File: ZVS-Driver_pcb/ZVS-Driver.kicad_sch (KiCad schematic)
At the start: 25 parts, among them J1 Screw_Terminal_01x02, J3 Screw_Terminal_01x04, Q1 IRF540N, Q2 IRF540N, Q3 IRF540N, Q4 IRF540N, Q5 IRF540N

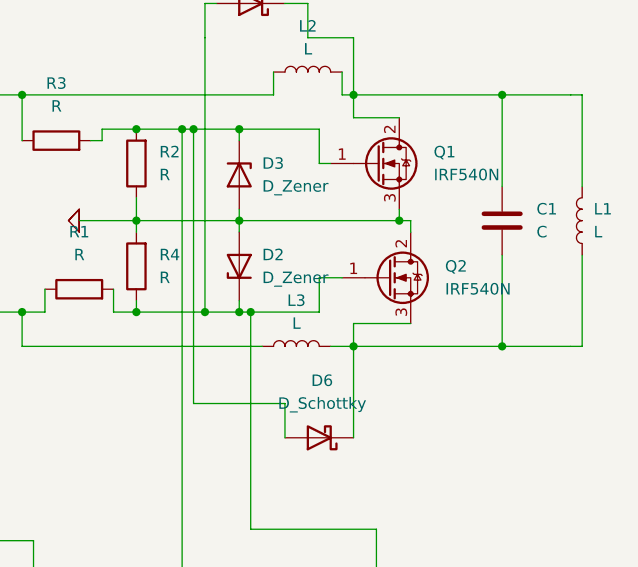
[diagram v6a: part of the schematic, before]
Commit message: Mosfet fix
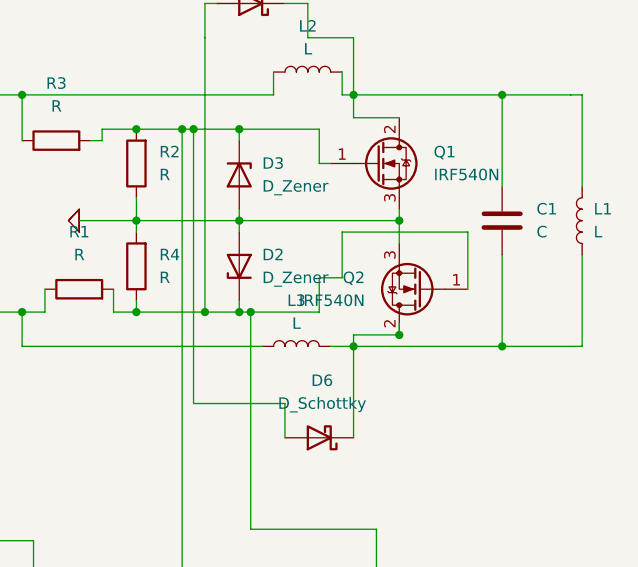
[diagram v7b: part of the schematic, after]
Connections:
- net 0: now also Q2.3 (S); no longer Q2.2 (D)
- net at C1.2, D6.1 (K), L1.1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: now also Q2.2 (D); no longer Q2.3 (S)
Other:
- moved on the sheet: Q2
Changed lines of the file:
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@@
 	)
 	(junction
+		(at 222.25 97.79)
+		(diameter 0)
+		(color 0 0 0 0)
+	)
+	(junction
 		(at 181.61 135.89)
 		(diameter 0)
@@
 	(wire
 		(pts
+			(xy 222.25 97.79) (xy 222.25 96.52)
+		)
+		(stroke
+			(width 0)
+			(type default)
+		)
+	)
+	(wire
+		(pts
 			(xy 135.89 97.79) (xy 135.89 93.98)
 		)
@@
 	(wire
 		(pts
+			(xy 229.87 86.36) (xy 215.9 86.36)
+		)
+		(stroke
+			(width 0)
+			(type default)
+		)
+	)
+	(wire
+		(pts
 			(xy 204.47 83.82) (xy 204.47 85.09)
 		)
@@
 	(wire
 		(pts
+			(xy 229.87 92.71) (xy 229.87 86.36)
+		)
+		(stroke
+			(width 0)
+			(type default)
+		)
+	)
+	(wire
+		(pts
 			(xy 242.57 81.28) (xy 242.57 71.12)
 		)
@@
 	(wire
 		(pts
-			(xy 217.17 96.52) (xy 223.52 96.52)
+			(xy 217.17 97.79) (xy 222.25 97.79)
 		)
 		(stroke
@@
 	(wire
 		(pts
-			(xy 223.52 86.36) (xy 223.52 85.09)
+			(xy 222.25 87.63) (xy 222.25 85.09)
 		)
 		(stroke
@@
 	(wire
 		(pts
+			(xy 215.9 86.36) (xy 215.9 91.44)
+		)
+		(stroke
+			(width 0)
+			(type default)
+		)
+	)
+	(wire
+		(pts
 			(xy 213.36 95.25) (xy 205.74 95.25)
 		)
@@
 	(wire
 		(pts
-			(xy 217.17 99.06) (xy 217.17 96.52)
+			(xy 217.17 99.06) (xy 217.17 97.79)
 		)
 		(stroke
@@
 	(wire
 		(pts
-			(xy 223.52 85.09) (xy 222.25 85.09)
-		)
-		(stroke
-			(width 0)
-			(type default)
-		)
-	)
-	(wire
-		(pts
 			(xy 213.36 74.93) (xy 213.36 78.74)
 		)
@@
 	(symbol
 		(lib_id "Transistor_FET:IRF540N")
-		(at 220.98 91.44 0)
+		(at 224.79 92.71 180)
 		(unit 1)
 		(exclude_from_sim no)
@@
 		(fields_autoplaced yes)
 		(property "Reference" "Q2"
-			(at 227.33 90.1699 0)
+			(at 218.44 91.4399 0)
 			(effects
 				(font
@@
 		)
 		(property "Value" "IRF540N"
-			(at 227.33 92.7099 0)
+			(at 218.44 93.9799 0)
 			(effects
 				(font
@@
 		)
 		(property "Footprint" "Package_TO_SOT_THT:TO-220-3_Vertical"
-			(at 226.06 93.345 0)
+			(at 219.71 90.805 0)
 			(effects
 				(font
@@
 		)
 		(property "Datasheet" "http://www.irf.com/product-info/datasheets/data/irf540n.pdf"
-			(at 226.06 95.25 0)
+			(at 219.71 88.9 0)
 			(effects
 				(font
@@
 		)
 		(property "Description" "33A Id, 100V Vds, HEXFET N-Channel MOSFET, TO-220"
-			(at 220.98 91.44 0)
+			(at 224.79 92.71 0)
 			(effects
 				(font
